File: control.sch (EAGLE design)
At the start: 4 parts, among them J1 1-2328702-0, U2 ESP32-DEVKITC-32D

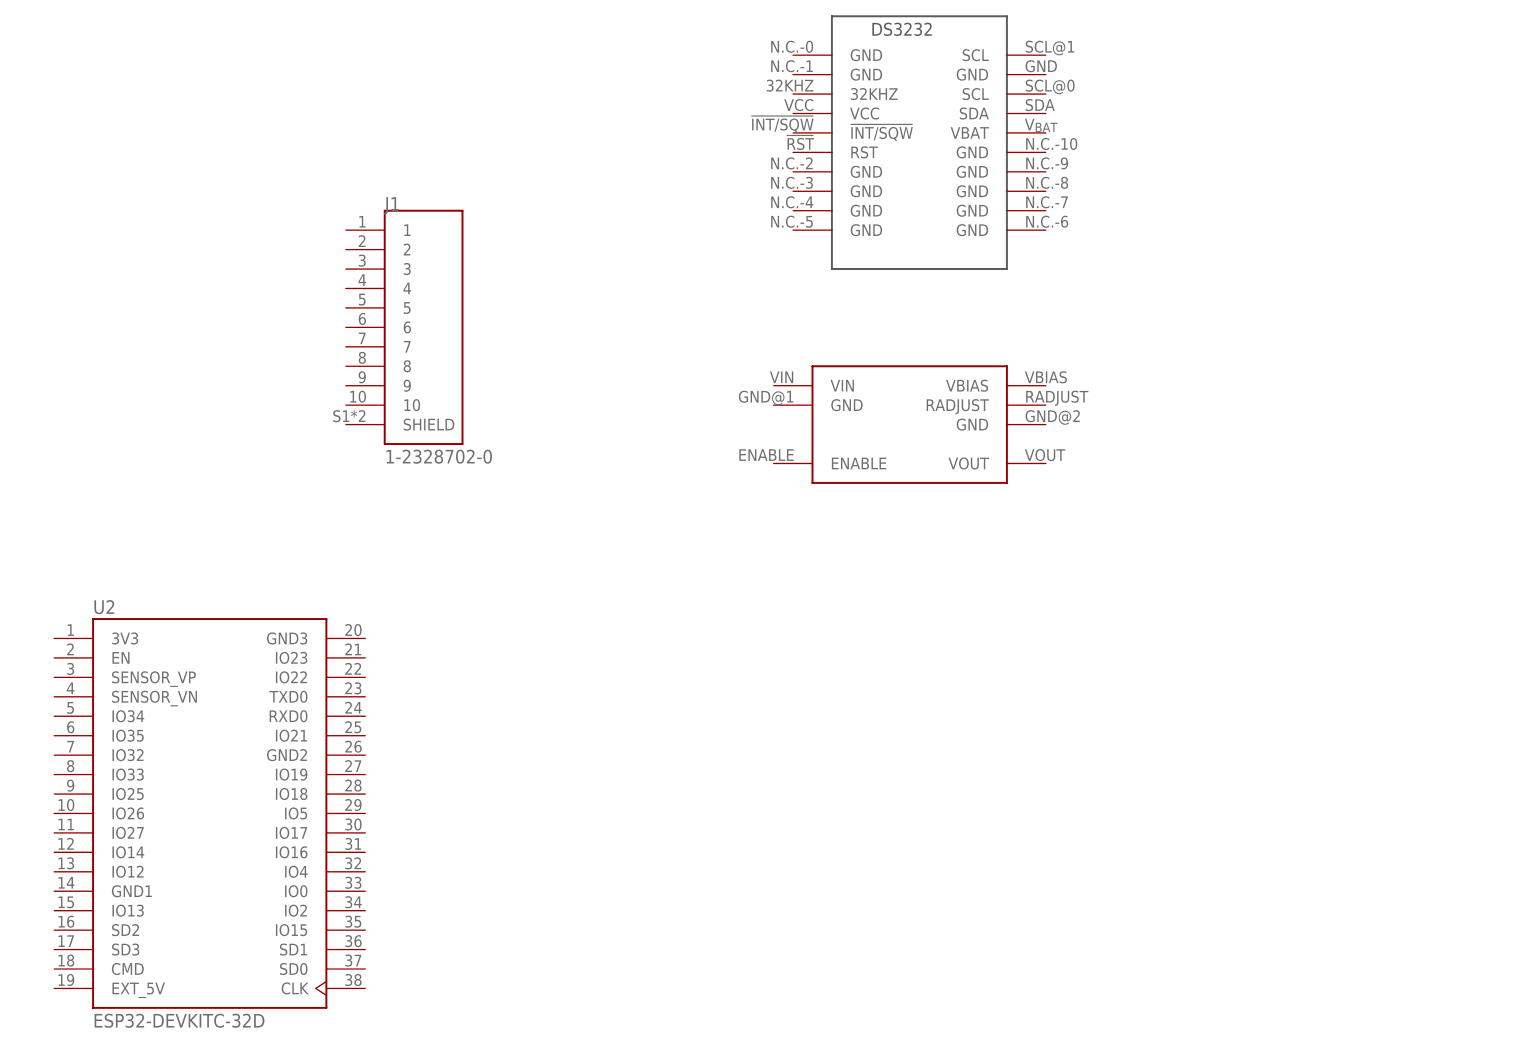
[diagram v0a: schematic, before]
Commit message: lamp board finished, working on control
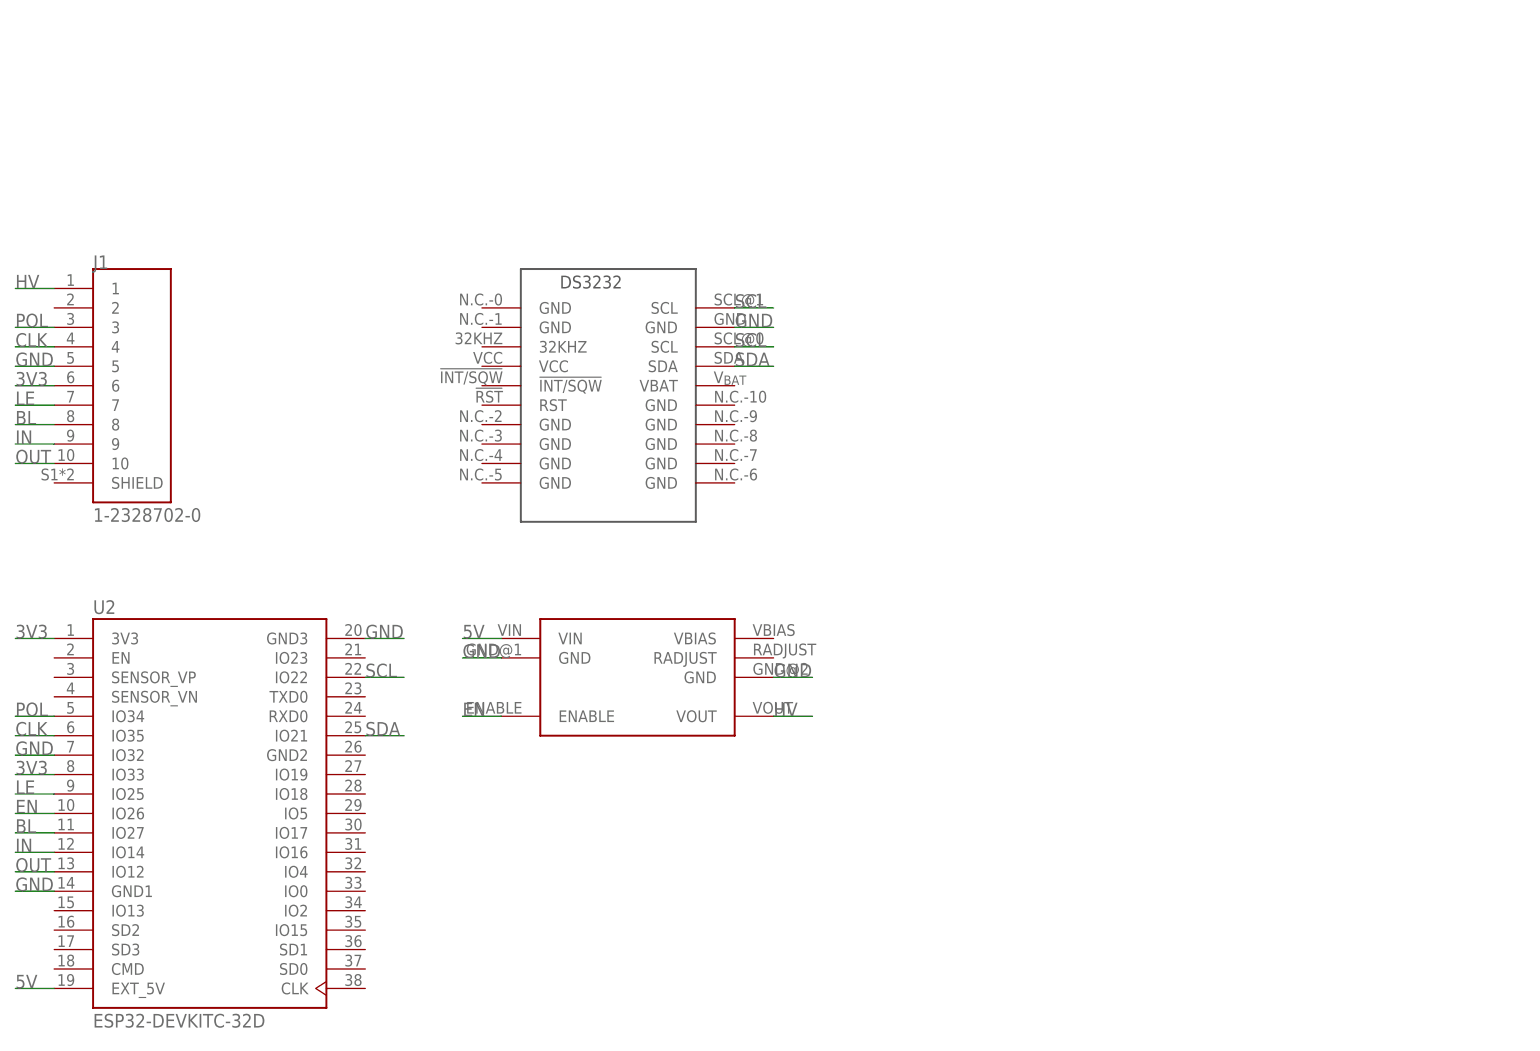
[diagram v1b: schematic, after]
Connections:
- new net 3V3: J1.6, U2.3V3, U2.IO33
- new net 5V: U$2.VIN, U2.EXT_5V
- new net BL: J1.8, U2.IO27
- new net CLK: J1.4, U2.IO35
- new net EN: U$2.ENABLE, U2.IO26
- new net GND: J1.5, U$1.GND@11, U$2.GND@1, U$2.GND@2, U2.GND1, U2.GND3, U2.IO32
- new net HV: J1.1, U$2.VOUT
- new net IN: J1.9, U2.IO14
- new net LE: J1.7, U2.IO25
- new net OUT: J1.10, U2.IO12
- new net POL: J1.3, U2.IO34
- new net SCL: U$1.SCL@0, U$1.SCL@1, U2.IO22
- new net SDA: U$1.SDA, U2.IO21
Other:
- moved on the sheet: J1
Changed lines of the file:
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@@
 </plain>
 <instances>
-<instance part="U$1" gate="G$1" x="276.86" y="147.32" smashed="yes"/>
-<instance part="U$2" gate="G$1" x="284.48" y="116.84" smashed="yes"/>
+<instance part="U$1" gate="G$1" x="236.22" y="114.3" smashed="yes"/>
+<instance part="U$2" gate="G$1" x="248.92" y="83.82" smashed="yes"/>
 <instance part="U2" gate="G$1" x="193.04" y="66.04" smashed="yes">
 <attribute name="NAME" x="177.7828" y="92.1043" size="1.78" layer="95"/>
 <attribute name="VALUE" x="177.7837" y="38.0702" size="1.7799" layer="96"/>
 </instance>
-<instance part="J1" gate="G$1" x="220.98" y="129.54" smashed="yes">
-<attribute name="NAME" x="215.9" y="144.78" size="1.778" layer="95"/>
-<attribute name="VALUE" x="215.9" y="111.76" size="1.778" layer="96"/>
+<instance part="J1" gate="G$1" x="182.88" y="121.92" smashed="yes">
+<attribute name="NAME" x="177.8" y="137.16" size="1.778" layer="95"/>
+<attribute name="VALUE" x="177.8" y="104.14" size="1.778" layer="96"/>
 </instance>
 </instances>
@@
 </busses>
 <nets>
+<net name="5V" class="0">
+<segment>
+<pinref part="U2" gate="G$1" pin="EXT_5V"/>
+<wire x1="172.72" y1="43.18" x2="167.64" y2="43.18" width="0.1524" layer="91"/>
+<label x="167.64" y="43.18" size="1.778" layer="95"/>
+</segment>
+<segment>
+<wire x1="231.14" y1="88.9" x2="226.06" y2="88.9" width="0.1524" layer="91"/>
+<label x="226.06" y="88.9" size="1.778" layer="95"/>
+<pinref part="U$2" gate="G$1" pin="VIN"/>
+</segment>
+</net>
+<net name="GND" class="0">
+<segment>
+<pinref part="U2" gate="G$1" pin="GND3"/>
+<wire x1="213.36" y1="88.9" x2="218.44" y2="88.9" width="0.1524" layer="91"/>
+<label x="213.36" y="88.9" size="1.778" layer="95"/>
+</segment>
+<segment>
+<wire x1="226.06" y1="86.36" x2="231.14" y2="86.36" width="0.1524" layer="91"/>
+<label x="226.06" y="86.36" size="1.778" layer="95"/>
+<pinref part="U$2" gate="G$1" pin="GND@1"/>
+</segment>
+<segment>
+<wire x1="266.7" y1="83.82" x2="271.78" y2="83.82" width="0.1524" layer="91"/>
+<label x="266.7" y="83.82" size="1.778" layer="95"/>
+<pinref part="U$2" gate="G$1" pin="GND@2"/>
+</segment>
+<segment>
+<wire x1="167.64" y1="55.88" x2="172.72" y2="55.88" width="0.1524" layer="91"/>
+<label x="167.64" y="55.88" size="1.778" layer="95"/>
+<pinref part="U2" gate="G$1" pin="GND1"/>
+</segment>
+<segment>
+<pinref part="J1" gate="G$1" pin="5"/>
+<wire x1="172.72" y1="124.46" x2="167.64" y2="124.46" width="0.1524" layer="91"/>
+<label x="167.64" y="124.46" size="1.778" layer="95"/>
+</segment>
+<segment>
+<wire x1="266.7" y1="129.54" x2="261.62" y2="129.54" width="0.1524" layer="91"/>
+<label x="261.62" y="129.54" size="1.778" layer="95"/>
+<pinref part="U$1" gate="G$1" pin="GND@11"/>
+</segment>
+<segment>
+<wire x1="172.72" y1="73.66" x2="167.64" y2="73.66" width="0.1524" layer="91"/>
+<label x="167.64" y="73.66" size="1.778" layer="95"/>
+<pinref part="U2" gate="G$1" pin="IO32"/>
+</segment>
+</net>
+<net name="3V3" class="0">
+<segment>
+<pinref part="U2" gate="G$1" pin="3V3"/>
+<wire x1="172.72" y1="88.9" x2="167.64" y2="88.9" width="0.1524" layer="91"/>
+<label x="167.64" y="88.9" size="1.778" layer="95"/>
+</segment>
+<segment>
+<pinref part="J1" gate="G$1" pin="6"/>
+<wire x1="172.72" y1="121.92" x2="167.64" y2="121.92" width="0.1524" layer="91"/>
+<label x="167.64" y="121.92" size="1.778" layer="95"/>
+</segment>
+<segment>
+<wire x1="172.72" y1="71.12" x2="167.64" y2="71.12" width="0.1524" layer="91"/>
+<label x="167.64" y="71.12" size="1.778" layer="95"/>
+<pinref part="U2" gate="G$1" pin="IO33"/>
+</segment>
+</net>
+<net name="HV" class="0">
+<segment>
+<pinref part="U$2" gate="G$1" pin="VOUT"/>
+<wire x1="266.7" y1="78.74" x2="271.78" y2="78.74" width="0.1524" layer="91"/>
+<label x="266.7" y="78.74" size="1.778" layer="95"/>
+</segment>
+<segment>
+<wire x1="167.64" y1="134.62" x2="172.72" y2="134.62" width="0.1524" layer="91"/>
+<label x="167.64" y="134.62" size="1.778" layer="95"/>
+<pinref part="J1" gate="G$1" pin="1"/>
+</segment>
+</net>
+<net name="POL" class="0">
+<segment>
+<pinref part="J1" gate="G$1" pin="3"/>
+<wire x1="172.72" y1="129.54" x2="167.64" y2="129.54" width="0.1524" layer="91"/>
+<label x="167.64" y="129.54" size="1.778" layer="95"/>
+</segment>
+<segment>
+<wire x1="172.72" y1="78.74" x2="167.64" y2="78.74" width="0.1524" layer="91"/>
+<label x="167.64" y="78.74" size="1.778" layer="95"/>
+<pinref part="U2" gate="G$1" pin="IO34"/>
+</segment>
+</net>
+<net name="CLK" class="0">
+<segment>
+<pinref part="J1" gate="G$1" pin="4"/>
+<wire x1="172.72" y1="127" x2="167.64" y2="127" width="0.1524" layer="91"/>
+<label x="167.64" y="127" size="1.778" layer="95"/>
+</segment>
+<segment>
+<wire x1="172.72" y1="76.2" x2="167.64" y2="76.2" width="0.1524" layer="91"/>
+<label x="167.64" y="76.2" size="1.778" layer="95"/>
+<pinref part="U2" gate="G$1" pin="IO35"/>
+</segment>
+</net>
+<net name="LE" class="0">
+<segment>
+<pinref part="J1" gate="G$1" pin="7"/>
+<wire x1="172.72" y1="119.38" x2="167.64" y2="119.38" width="0.1524" layer="91"/>
+<label x="167.64" y="119.38" size="1.778" layer="95"/>
+</segment>
+<segment>
+<wire x1="172.72" y1="68.58" x2="167.64" y2="68.58" width="0.1524" layer="91"/>
+<label x="167.64" y="68.58" size="1.778" layer="95"/>
+<pinref part="U2" gate="G$1" pin="IO25"/>
+</segment>
+</net>
+<net name="BL" class="0">
+<segment>
+<pinref part="J1" gate="G$1" pin="8"/>
+<wire x1="172.72" y1="116.84" x2="167.64" y2="116.84" width="0.1524" layer="91"/>
+<label x="167.64" y="116.84" size="1.778" layer="95"/>
+</segment>
+<segment>
+<wire x1="172.72" y1="63.5" x2="167.64" y2="63.5" width="0.1524" layer="91"/>
+<label x="167.64" y="63.5" size="1.778" layer="95"/>
+<pinref part="U2" gate="G$1" pin="IO27"/>
+</segment>
+</net>
+<net name="IN" class="0">
+<segment>
+<pinref part="J1" gate="G$1" pin="9"/>
+<wire x1="172.72" y1="114.3" x2="167.64" y2="114.3" width="0.1524" layer="91"/>
+<label x="167.64" y="114.3" size="1.778" layer="95"/>
+</segment>
+<segment>
+<wire x1="172.72" y1="60.96" x2="167.64" y2="60.96" width="0.1524" layer="91"/>
+<label x="167.64" y="60.96" size="1.778" layer="95"/>
+<pinref part="U2" gate="G$1" pin="IO14"/>
+</segment>
+</net>
+<net name="OUT" class="0">
+<segment>
+<pinref part="J1" gate="G$1" pin="10"/>
+<wire x1="172.72" y1="111.76" x2="167.64" y2="111.76" width="0.1524" layer="91"/>
+<label x="167.64" y="111.76" size="1.778" layer="95"/>
+</segment>
+<segment>
+<wire x1="172.72" y1="58.42" x2="167.64" y2="58.42" width="0.1524" layer="91"/>
+<label x="167.64" y="58.42" size="1.778" layer="95"/>
+<pinref part="U2" gate="G$1" pin="IO12"/>
+</segment>
+</net>
+<net name="EN" class="0">
+<segment>
+<pinref part="U$2" gate="G$1" pin="ENABLE"/>
+<wire x1="231.14" y1="78.74" x2="226.06" y2="78.74" width="0.1524" layer="91"/>
+<label x="226.06" y="78.74" size="1.778" layer="95"/>
+</segment>
+<segment>
+<wire x1="172.72" y1="66.04" x2="167.64" y2="66.04" width="0.1524" layer="91"/>
+<label x="167.64" y="66.04" size="1.778" layer="95"/>
+<pinref part="U2" gate="G$1" pin="IO26"/>
+</segment>
+</net>
+<net name="SCL" class="0">
+<segment>
+<pinref part="U$1" gate="G$1" pin="SCL@1"/>
+<wire x1="261.62" y1="132.08" x2="266.7" y2="132.08" width="0.1524" layer="91"/>
+<label x="261.62" y="132.08" size="1.778" layer="95"/>
+</segment>
+<segment>
+<wire x1="261.62" y1="127" x2="266.7" y2="127" width="0.1524" layer="91"/>
+<label x="261.62" y="127" size="1.778" layer="95"/>
+<pinref part="U$1" gate="G$1" pin="SCL@0"/>
+</segment>
+<segment>
+<wire x1="213.36" y1="83.82" x2="218.44" y2="83.82" width="0.1524" layer="91"/>
+<label x="213.36" y="83.82" size="1.778" layer="95"/>
+<pinref part="U2" gate="G$1" pin="IO22"/>
+</segment>
+</net>
+<net name="SDA" class="0">
+<segment>
+<pinref part="U$1" gate="G$1" pin="SDA"/>
+<wire x1="261.62" y1="124.46" x2="266.7" y2="124.46" width="0.1524" layer="91"/>
+<label x="261.62" y="124.46" size="1.778" layer="95"/>
+</segment>
+<segment>
+<wire x1="213.36" y1="76.2" x2="218.44" y2="76.2" width="0.1524" layer="91"/>
+<label x="213.36" y="76.2" size="1.778" layer="95"/>
+<pinref part="U2" gate="G$1" pin="IO21"/>
+</segment>
+</net>
 </nets>
 </sheet>
